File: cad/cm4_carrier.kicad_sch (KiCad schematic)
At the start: 24 parts, among them J1 5V_IN, J2 CM4, J3 RS485, J4 USB_DEBUG, J5 I2C, J6 SPI, J7 GPIO, Q1 SI2301, U1 MAX3485, U2 CP2102N

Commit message: 🐛 fix: correct CP2102N footprint to QFN-20 4x4mm
The 3x3mm QFN-20 footprint doesn't exist in KiCad libraries.
CP2102N uses QFN-20-1EP_4x4mm_P0.5mm_EP2.5x2.5mm.

Co-Authored-By: Claude Opus 4.6 (1M context) <noreply@anthropic.com>
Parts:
- U2: footprint Package_DFN_QFN:QFN-20-1EP_3x3mm_P0.5mm_EP1.7x1.7mm -> Package_DFN_QFN:QFN-20-1EP_4x4mm_P0.5mm_EP2.5x2.5mm
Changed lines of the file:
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@@
 		(instances
 			(project "CM4_Carrier"
-				(path "/45eae081-659c-47a5-acb9-86ef63c0ae42"
+				(path "/e7cc9dbb-b043-429b-8f75-bc756f5a2e8c"
 					(reference "#PWR01")
 					(unit 1)
@@
 		(instances
 			(project "CM4_Carrier"
-				(path "/45eae081-659c-47a5-acb9-86ef63c0ae42"
+				(path "/e7cc9dbb-b043-429b-8f75-bc756f5a2e8c"
 					(reference "#PWR02")
 					(unit 1)
@@
 		(instances
 			(project "CM4_Carrier"
-				(path "/45eae081-659c-47a5-acb9-86ef63c0ae42"
+				(path "/e7cc9dbb-b043-429b-8f75-bc756f5a2e8c"
 					(reference "J1")
 					(unit 1)
@@
 		(instances
 			(project "CM4_Carrier"
-				(path "/45eae081-659c-47a5-acb9-86ef63c0ae42"
+				(path "/e7cc9dbb-b043-429b-8f75-bc756f5a2e8c"
 					(reference "F1")
 					(unit 1)
@@
 		(instances
 			(project "CM4_Carrier"
-				(path "/45eae081-659c-47a5-acb9-86ef63c0ae42"
+				(path "/e7cc9dbb-b043-429b-8f75-bc756f5a2e8c"
 					(reference "Q1")
 					(unit 1)
@@
 		(instances
 			(project "CM4_Carrier"
-				(path "/45eae081-659c-47a5-acb9-86ef63c0ae42"
+				(path "/e7cc9dbb-b043-429b-8f75-bc756f5a2e8c"
 					(reference "C1")
 					(unit 1)
@@
 		(instances
 			(project "CM4_Carrier"
-				(path "/45eae081-659c-47a5-acb9-86ef63c0ae42"
+				(path "/e7cc9dbb-b043-429b-8f75-bc756f5a2e8c"
 					(reference "C2")
 					(unit 1)
@@
 		(instances
 			(project "CM4_Carrier"
-				(path "/45eae081-659c-47a5-acb9-86ef63c0ae42"
+				(path "/e7cc9dbb-b043-429b-8f75-bc756f5a2e8c"
 					(reference "#FLG01")
 					(unit 1)
@@
 		(instances
 			(project "CM4_Carrier"
-				(path "/45eae081-659c-47a5-acb9-86ef63c0ae42"
+				(path "/e7cc9dbb-b043-429b-8f75-bc756f5a2e8c"
 					(reference "#FLG02")
 					(unit 1)
@@
 		(instances
 			(project "CM4_Carrier"
-				(path "/45eae081-659c-47a5-acb9-86ef63c0ae42"
+				(path "/e7cc9dbb-b043-429b-8f75-bc756f5a2e8c"
 					(reference "J2")
 					(unit 1)
@@
 		(instances
 			(project "CM4_Carrier"
-				(path "/45eae081-659c-47a5-acb9-86ef63c0ae42"
+				(path "/e7cc9dbb-b043-429b-8f75-bc756f5a2e8c"
 					(reference "U1")
 					(unit 1)
@@
 		(instances
 			(project "CM4_Carrier"
-				(path "/45eae081-659c-47a5-acb9-86ef63c0ae42"
+				(path "/e7cc9dbb-b043-429b-8f75-bc756f5a2e8c"
 					(reference "R1")
 					(unit 1)
@@
 		(instances
 			(project "CM4_Carrier"
-				(path "/45eae081-659c-47a5-acb9-86ef63c0ae42"
+				(path "/e7cc9dbb-b043-429b-8f75-bc756f5a2e8c"
 					(reference "R2")
 					(unit 1)
@@
 		(instances
 			(project "CM4_Carrier"
-				(path "/45eae081-659c-47a5-acb9-86ef63c0ae42"
+				(path "/e7cc9dbb-b043-429b-8f75-bc756f5a2e8c"
 					(reference "R3")
 					(unit 1)
@@
 		(instances
 			(project "CM4_Carrier"
-				(path "/45eae081-659c-47a5-acb9-86ef63c0ae42"
+				(path "/e7cc9dbb-b043-429b-8f75-bc756f5a2e8c"
 					(reference "J3")
 					(unit 1)
@@
 		(instances
 			(project "CM4_Carrier"
-				(path "/45eae081-659c-47a5-acb9-86ef63c0ae42"
+				(path "/e7cc9dbb-b043-429b-8f75-bc756f5a2e8c"
 					(reference "C3")
 					(unit 1)
@@
 			)
 		)
-		(property "Footprint" "Package_DFN_QFN:QFN-20-1EP_3x3mm_P0.5mm_EP1.7x1.7mm"
+		(property "Footprint" "Package_DFN_QFN:QFN-20-1EP_4x4mm_P0.5mm_EP2.5x2.5mm"
 			(at 133.35 30.48 0.0000)
 			(effects
@@
 		(instances
 			(project "CM4_Carrier"
-				(path "/45eae081-659c-47a5-acb9-86ef63c0ae42"
+				(path "/e7cc9dbb-b043-429b-8f75-bc756f5a2e8c"
 					(reference "U2")
 					(unit 1)
@@
 		(instances
 			(project "CM4_Carrier"
-				(path "/45eae081-659c-47a5-acb9-86ef63c0ae42"
+				(path "/e7cc9dbb-b043-429b-8f75-bc756f5a2e8c"
 					(reference "J4")
 					(unit 1)
@@
 		(instances
 			(project "CM4_Carrier"
-				(path "/45eae081-659c-47a5-acb9-86ef63c0ae42"
+				(path "/e7cc9dbb-b043-429b-8f75-bc756f5a2e8c"
 					(reference "C4")
 					(unit 1)
@@
 		(instances
 			(project "CM4_Carrier"
-				(path "/45eae081-659c-47a5-acb9-86ef63c0ae42"
+				(path "/e7cc9dbb-b043-429b-8f75-bc756f5a2e8c"
 					(reference "R4")
 					(unit 1)
@@
 		(instances
 			(project "CM4_Carrier"
-				(path "/45eae081-659c-47a5-acb9-86ef63c0ae42"
+				(path "/e7cc9dbb-b043-429b-8f75-bc756f5a2e8c"
 					(reference "R5")
 					(unit 1)
@@
 		(instances
 			(project "CM4_Carrier"
-				(path "/45eae081-659c-47a5-acb9-86ef63c0ae42"
+				(path "/e7cc9dbb-b043-429b-8f75-bc756f5a2e8c"
 					(reference "J5")
 					(unit 1)
@@
 		(instances
 			(project "CM4_Carrier"
-				(path "/45eae081-659c-47a5-acb9-86ef63c0ae42"
+				(path "/e7cc9dbb-b043-429b-8f75-bc756f5a2e8c"
 					(reference "J6")
 					(unit 1)
@@
 		(instances
 			(project "CM4_Carrier"
-				(path "/45eae081-659c-47a5-acb9-86ef63c0ae42"
+				(path "/e7cc9dbb-b043-429b-8f75-bc756f5a2e8c"
 					(reference "J7")
 					(unit 1)
@@
 		(instances
 			(project "CM4_Carrier"
-				(path "/45eae081-659c-47a5-acb9-86ef63c0ae42"
+				(path "/e7cc9dbb-b043-429b-8f75-bc756f5a2e8c"
 					(reference "C5")
 					(unit 1)
@@
 		(instances
 			(project "CM4_Carrier"
-				(path "/45eae081-659c-47a5-acb9-86ef63c0ae42"
+				(path "/e7cc9dbb-b043-429b-8f75-bc756f5a2e8c"
 					(reference "C6")
 					(unit 1)
@@
 		(instances
 			(project "CM4_Carrier"
-				(path "/45eae081-659c-47a5-acb9-86ef63c0ae42"
+				(path "/e7cc9dbb-b043-429b-8f75-bc756f5a2e8c"
 					(reference "C7")
 					(unit 1)
@@
 		(instances
 			(project "CM4_Carrier"
-				(path "/45eae081-659c-47a5-acb9-86ef63c0ae42"
+				(path "/e7cc9dbb-b043-429b-8f75-bc756f5a2e8c"
 					(reference "C8")
 					(unit 1)

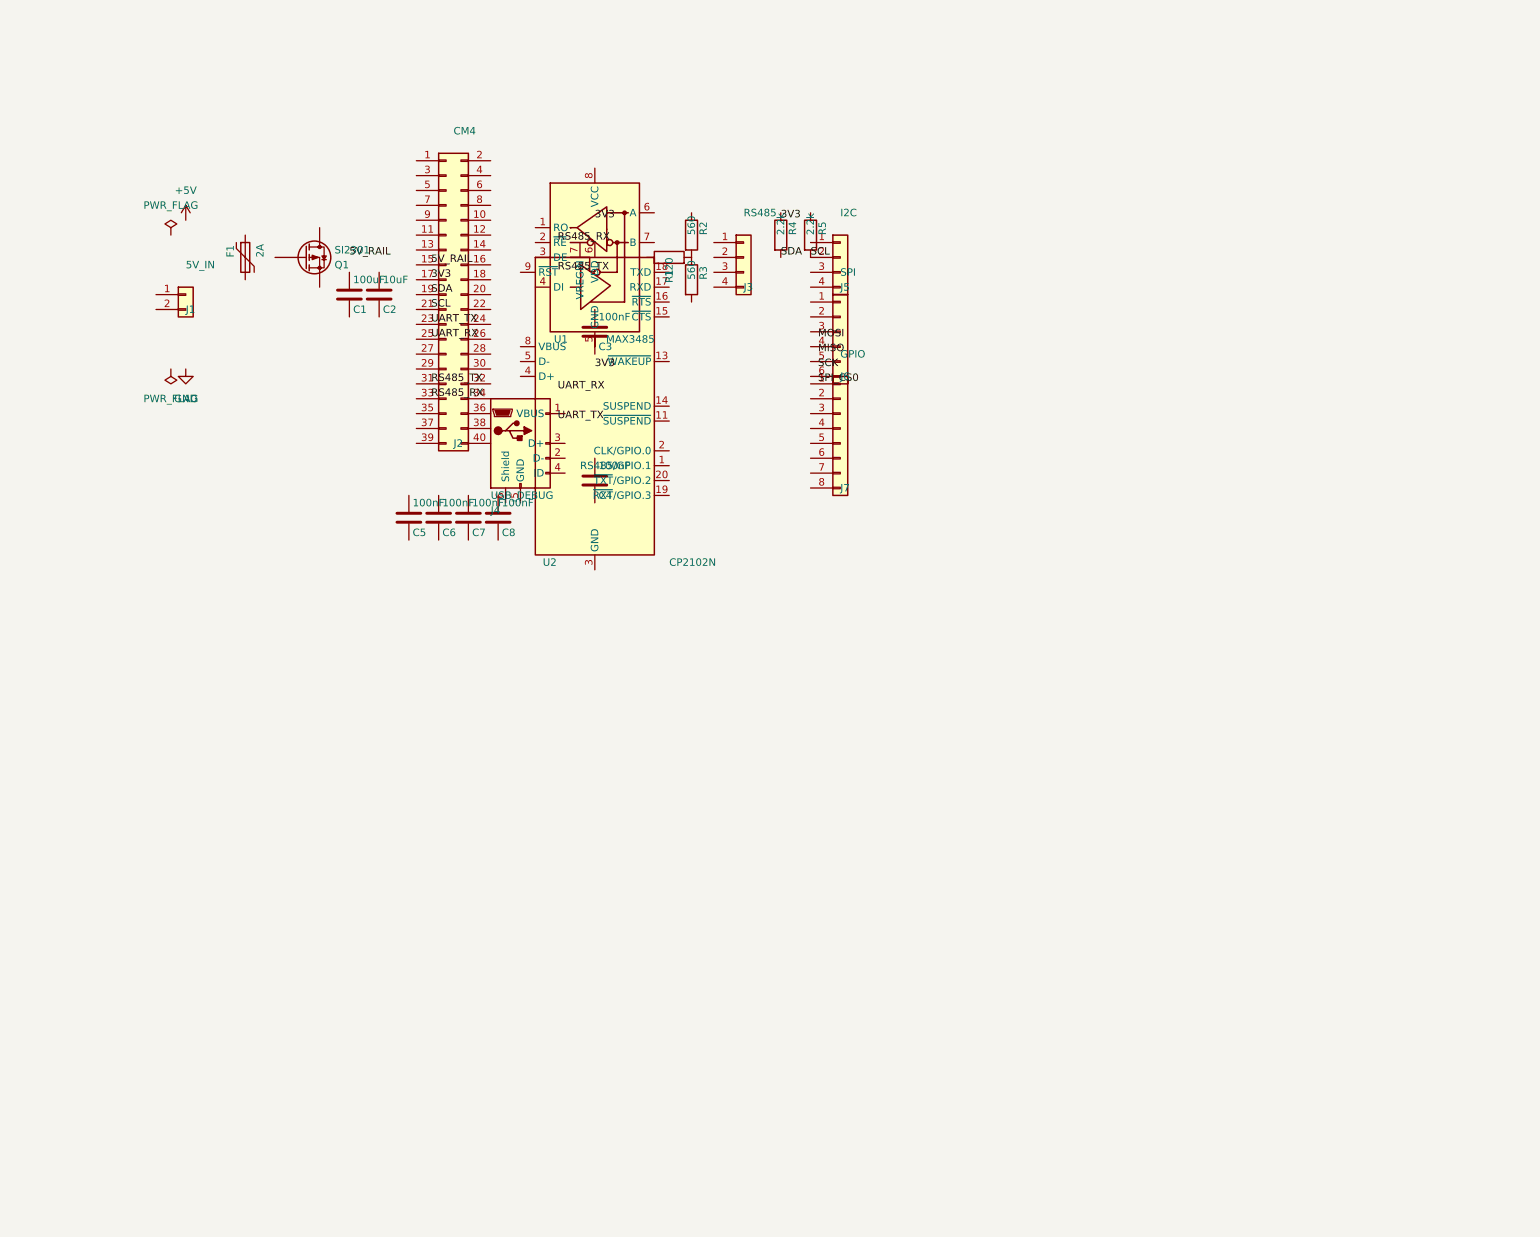
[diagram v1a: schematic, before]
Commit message: ✨ feat: layout-spec-driven schematic with visual review
Schematic generation now reads cad/layout_spec.yaml for block positions.
Six blocks with clear separation: power (top-left), CM4 (top-center),
RS-485 (top-right), USB-UART (bot-left), decoupling (bot-center),
I/O headers (bot-right). Power symbols at top, GND at bottom per block.
Visual review confirms legible layout with no major overlaps.

Co-Authored-By: Claude Opus 4.6 (1M context) <noreply@anthropic.com>
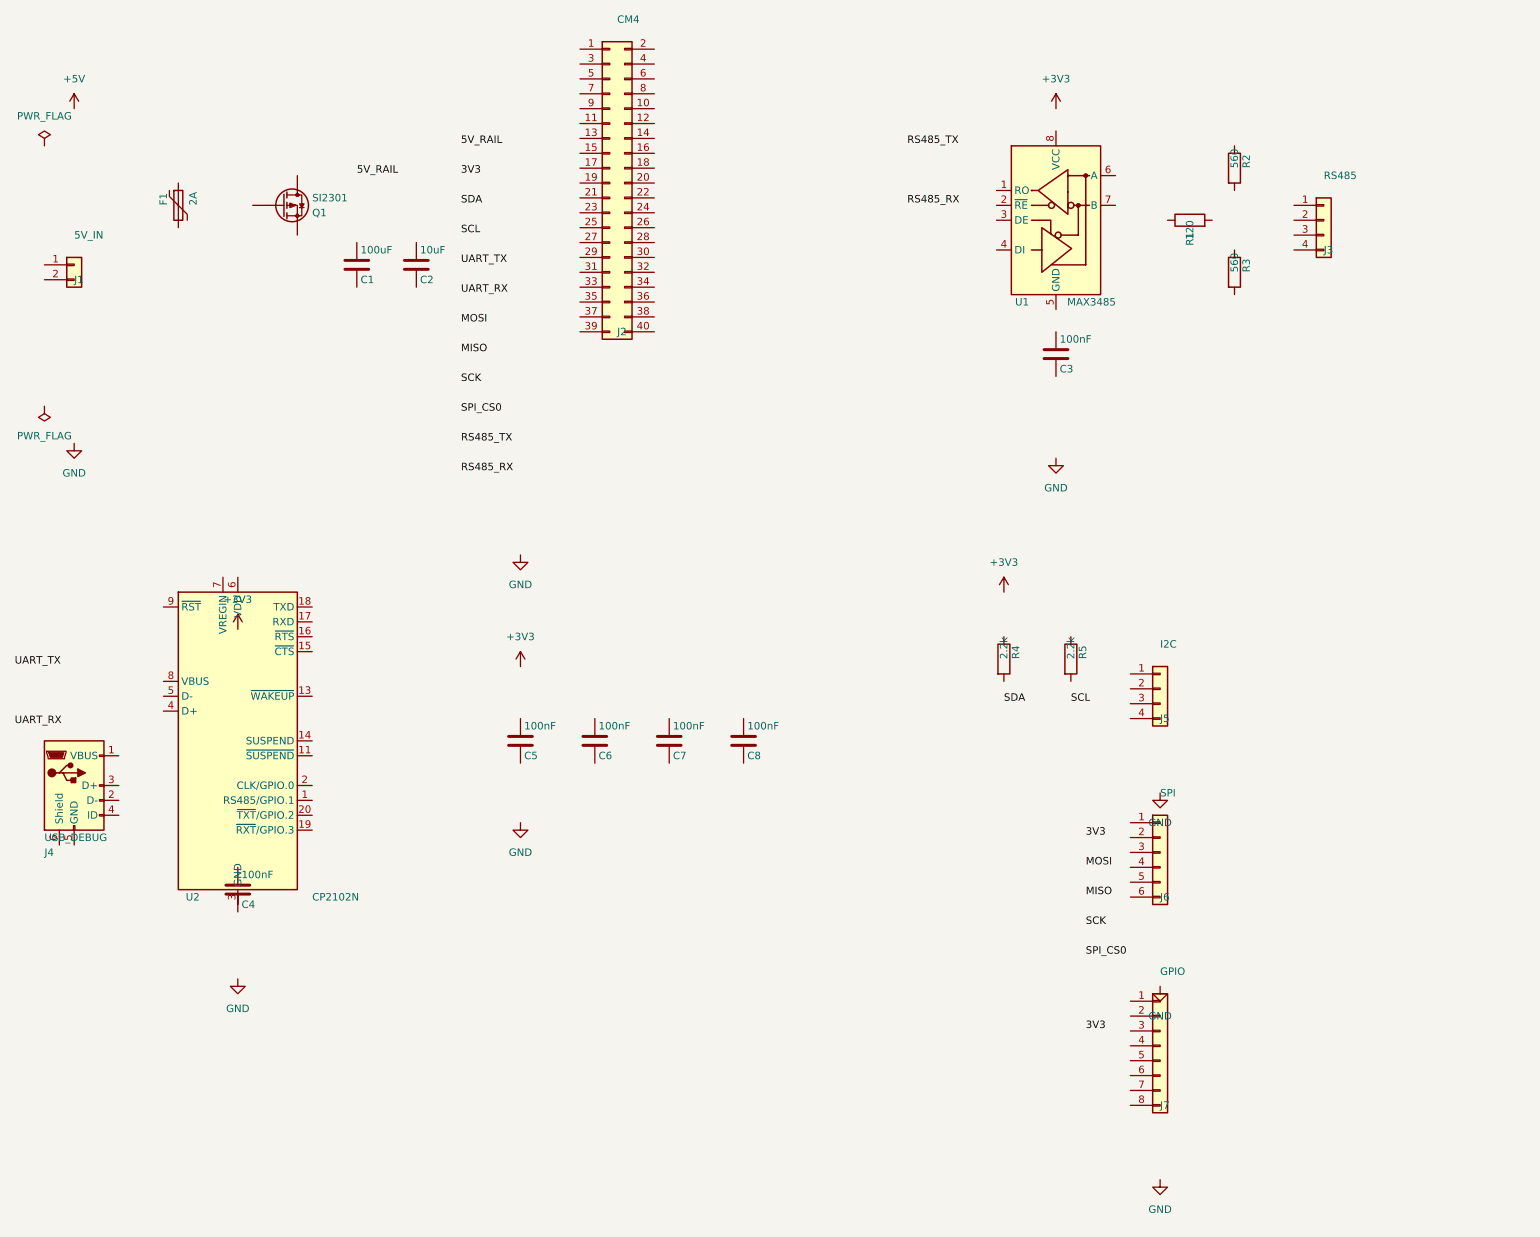
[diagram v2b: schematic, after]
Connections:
- net SCL: no longer J5.2 (Pin_2), R5.2
- net SDA: no longer R4.2
- now unconnected: R1.2, R2.2, R3.1

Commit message: ✨ feat: full code-to-fabrication pipeline with /generate-schematic skill
- Split cad/ into netlist/ (source) and schematic/ (generated, gitignored)
- Add generate-model/generate-asm poe tasks (replace drawings), align EE+ME
- Add validate-asm (DRC) alongside validate-model (ERC)
- Move output from spec/drawings/ to output/ (drawings/, gerbers/, STEP)
- Sheet size from layout_spec.yaml (A3), %Z auto-fills drawing sheet
- Margin offset (30,28) clears sheet border
- Y-coordinate coincidence bug workaround for KiCad ERC
- SKILL.md with all lessons learned, ships with repo
- readme documents full workflow: /generate-schematic → validate → inspect → generate

Co-Authored-By: Claude Opus 4.6 (1M context) <noreply@anthropic.com>
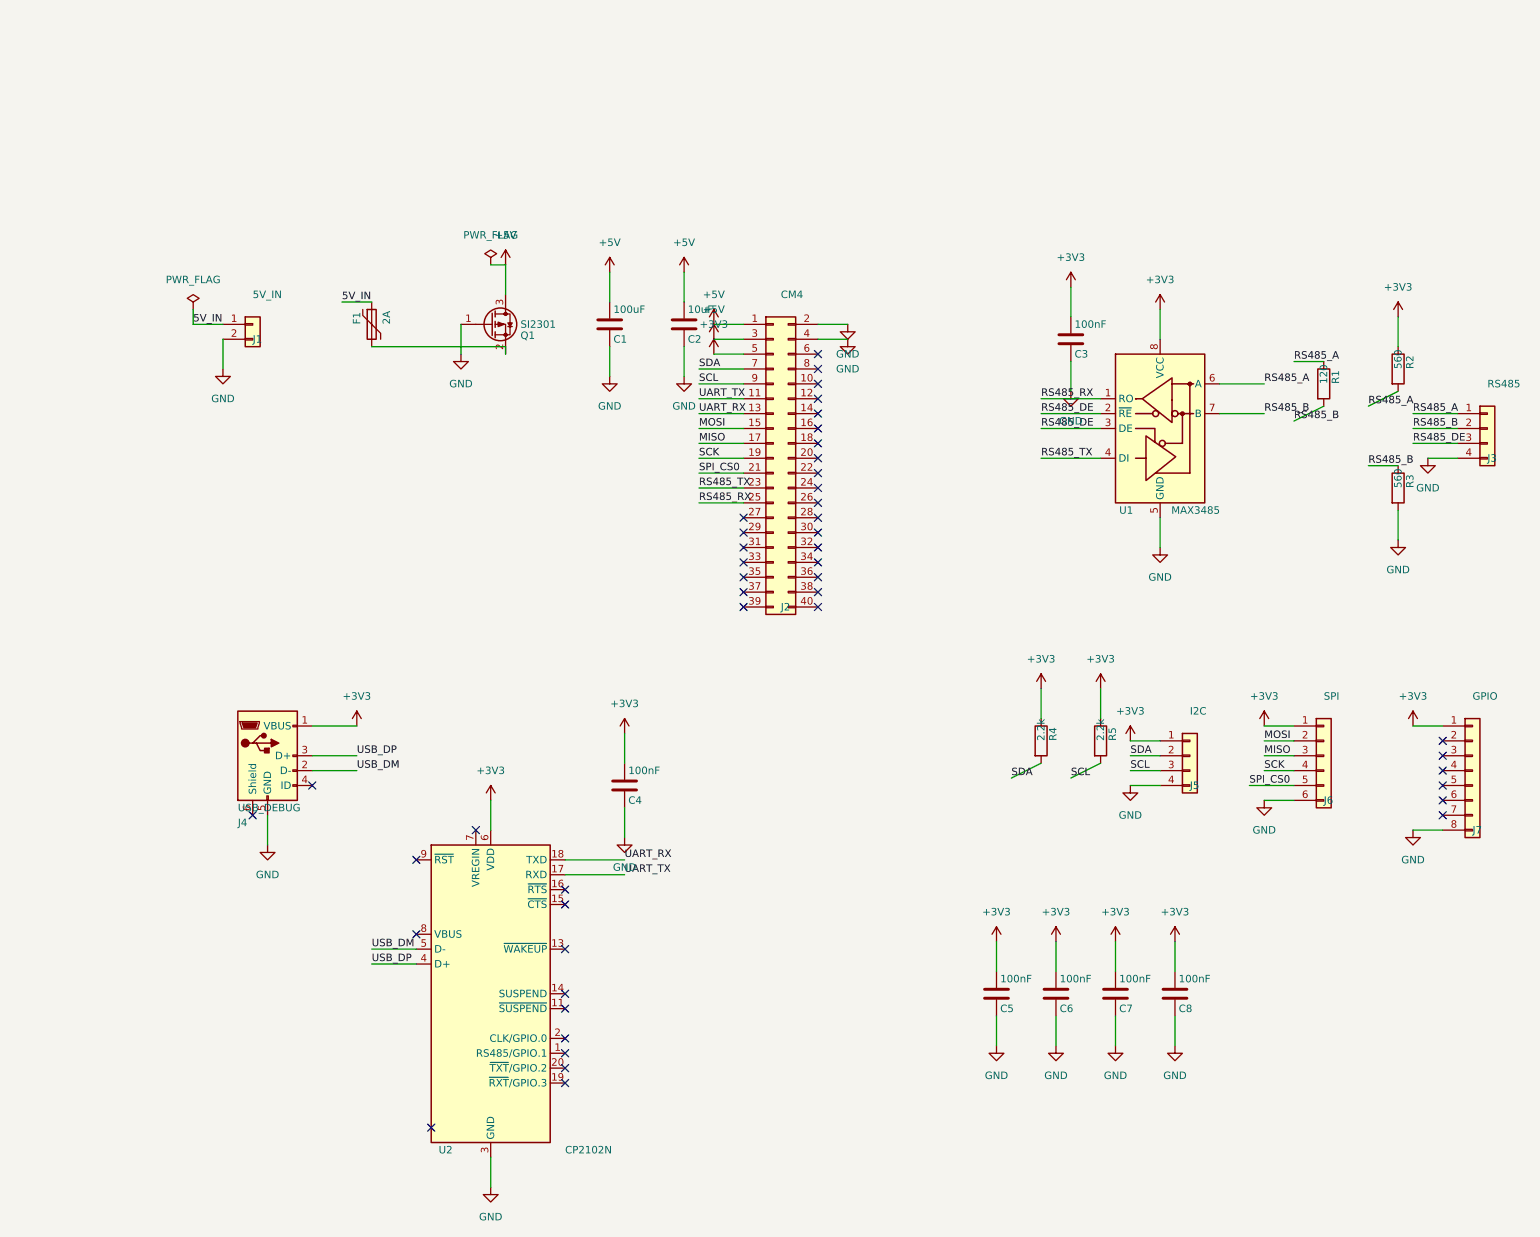
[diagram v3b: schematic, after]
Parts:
- removed Q1: SI2301, Package_TO_SOT_SMD:SOT-23, symbol Device:Q_PMOS
- added Q1: SI2301, Package_TO_SOT_SMD:SOT-23, symbol Transistor_FET:Q_PMOS_GSD
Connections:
- net +3V3: now also C3.1, C4.1, C5.1, C6.1, C7.1, C8.1, J2.5 (Pin_5), J4.1 (VBUS), J5.1 (Pin_1), J6.1 (Pin_1), J7.1 (Pin_1), R2.1, R4.1, R5.1, U1.8 (VCC), U2.6 (VDD)
- net +5V: now also C1.1, C2.1, J2.1 (Pin_1), J2.3 (Pin_3), Q1.3 (D)
- net GND: now also C1.2, C2.2, C3.2, C4.2, C5.2, C6.2, C7.2, C8.2, J1.2 (Pin_2), J2.2 (Pin_2), J2.4 (Pin_4), J3.4 (Pin_4), J4.5 (GND), J5.4 (Pin_4), J6.6 (Pin_6), J7.8 (Pin_8), R3.2, U1.5 (GND), U2.12 (GND), U2.21 (GND), U2.3 (GND), Q1.1 (G)
- net MISO: now also J2.17 (Pin_17), J6.3 (Pin_3)
- net MOSI: now also J2.15 (Pin_15), J6.2 (Pin_2)
- net RS485_RX: now also J2.25 (Pin_25), U1.1 (RO)
- net RS485_TX: now also J2.23 (Pin_23), U1.4 (DI)
- net SCK: now also J2.19 (Pin_19), J6.4 (Pin_4)
- net SCL: now also J2.9 (Pin_9), J5.3 (Pin_3), R5.2
- net SDA: now also J2.7 (Pin_7), J5.2 (Pin_2), R4.2
- net SPI_CS0: now also J2.21 (Pin_21), J6.5 (Pin_5)
- net UART_RX: now also J2.13 (Pin_13), U2.18 (TXD)
- net UART_TX: now also J2.11 (Pin_11), U2.17 (RXD)
- net USB_DP: now reaches U2.4 (D+)
- net USB_DP: now also J4.3 (D+)
- net USB_DM: now reaches U2.5 (D-)
- net USB_DM: now also J4.2 (D-)
- net RS485_DE: now reaches U1.2 (~{RE})
- net RS485_DE: now also J3.3 (Pin_3), U1.3 (DE)
- net RS485_A: now reaches U1.6 (A)
- net RS485_A: now also J3.1 (Pin_1), R1.1, R2.2
- net RS485_B: now reaches U1.7 (B)
- net RS485_B: now also J3.2 (Pin_2), R1.2, R3.1
- net 5V_IN: now reaches J1.1 (Pin_1)
- net 5V_IN: now also F1.1
- net at F1.2: now also Q1.2 (S)
- no-connect marks 0 -> 46
